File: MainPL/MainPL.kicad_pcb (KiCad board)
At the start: 2 copper layers, 113 x 155.6 mm, 37 parts, among them J1 Conn_01x06_Female, J10 Conn_01x06_Female, J11 Conn_01x06_Female, J12 Conn_01x06_Female, J13 Conn_01x06_Female, J14 Conn_01x06_Female, J15 Conn_01x01_Male, J16 Conn_01x04_Male, J2 USB_B, J3 Conn_01x06_Female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

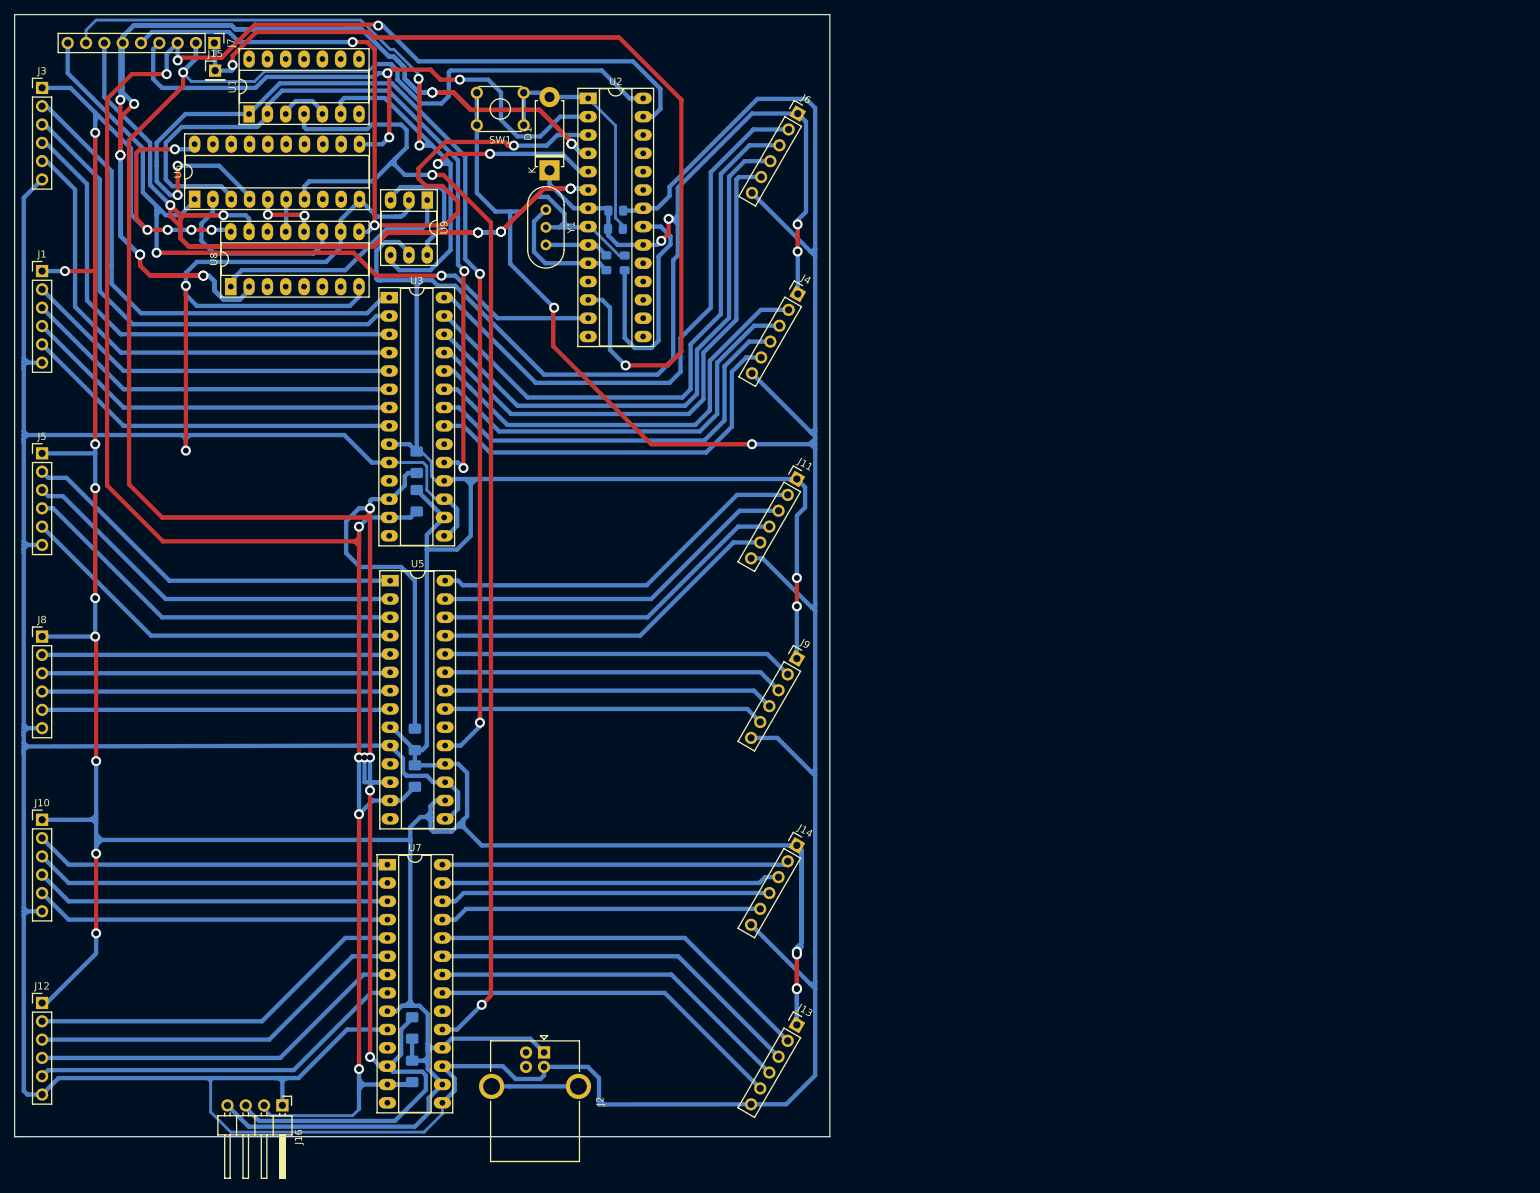
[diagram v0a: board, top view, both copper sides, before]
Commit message: Änderung der Ints und leichte Verbesserung
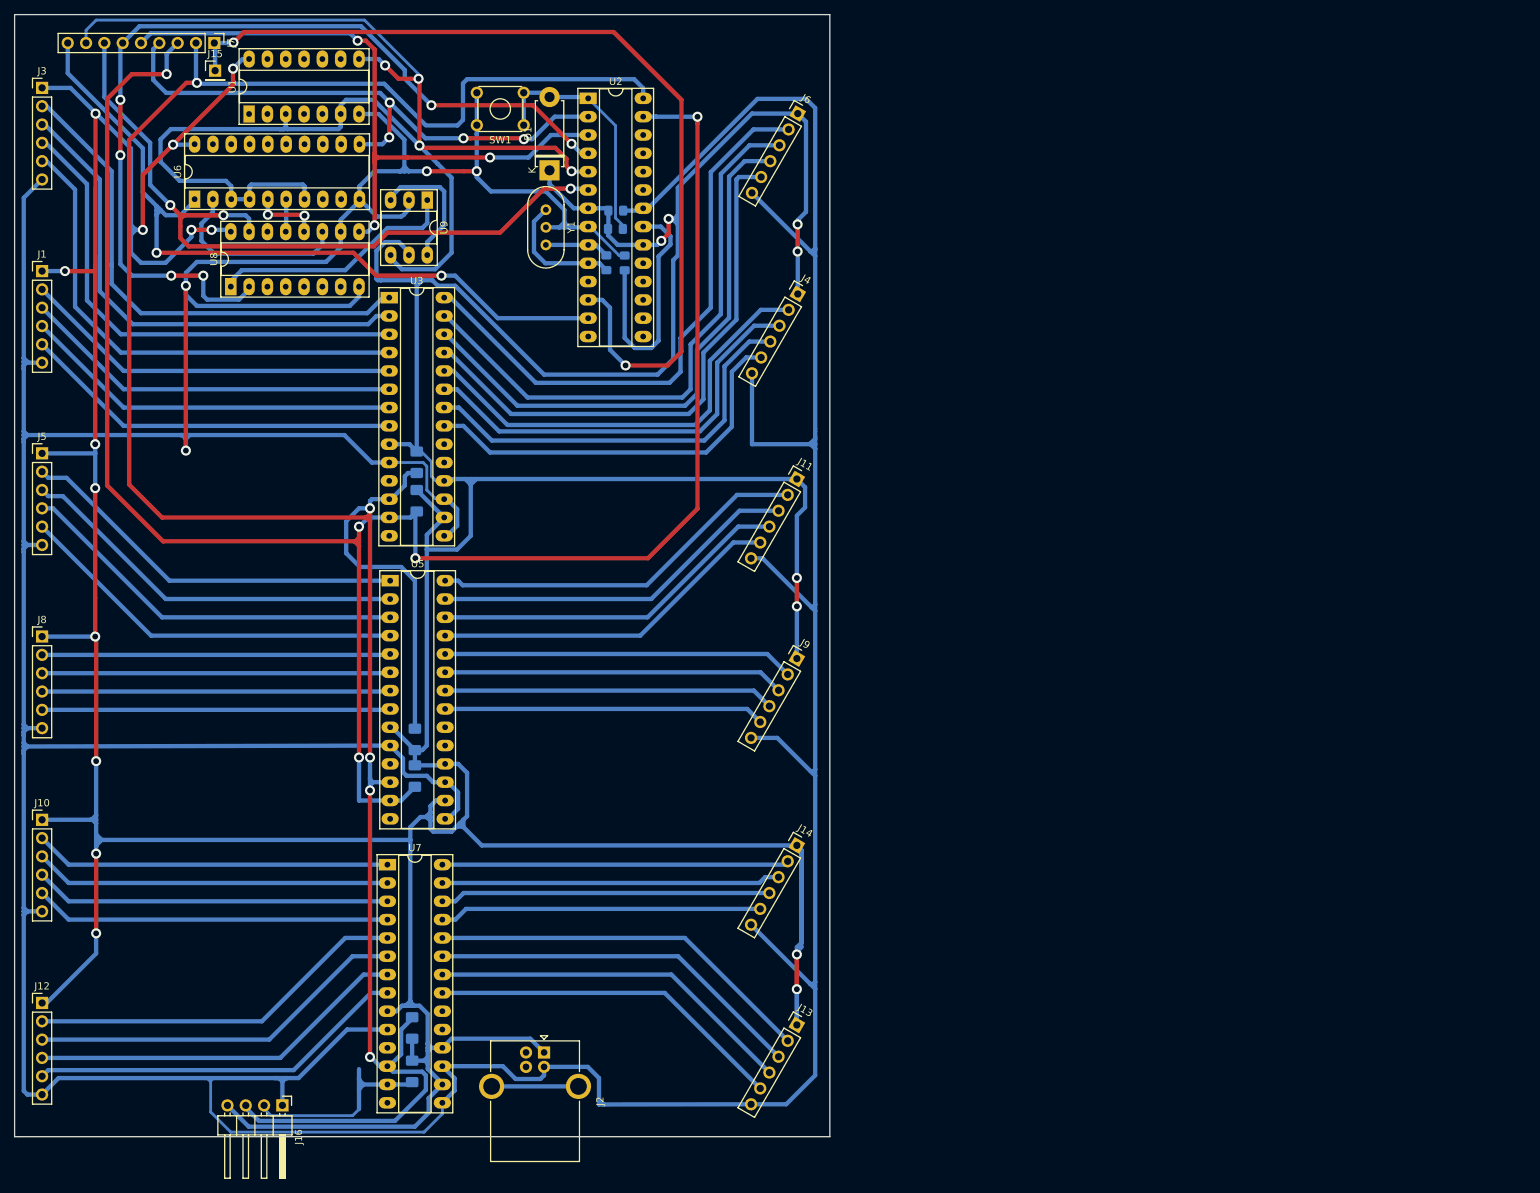
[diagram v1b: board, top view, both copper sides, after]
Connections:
- U1 pad 1: /INTB_2 -> Net-(U1-Pad1)
- U1 pad 10: (no net) -> Net-(U1-Pad10)
- U1 pad 14: (no net) -> +5V
- U1 pad 2: /INTB_1 -> Net-(U1-Pad2)
- U1 pad 3: Net-(U1-Pad3) -> /INTArduino
- U1 pad 4: /INTB_3 -> Net-(U1-Pad4)
- U1 pad 5: Net-(U1-Pad3) -> /INTB_2
- U1 pad 7: (no net) -> GND
- U1 pad 8: (no net) -> /INTArduino
- U1 pad 9: (no net) -> Net-(U1-Pad9)
- U3 pad 19: /INTB_1 -> Net-(U1-Pad2)
- U3 pad 20: Net-(U3-Pad20) -> Net-(U1-Pad1)
- U5 pad 20: Net-(U5-Pad20) -> Net-(U1-Pad4)
- U6 pad 3: /INTB_1 -> /INTArduino
- U6 pad 4: /INTB_2 -> /INTArduino
- U6 pad 7: /INTB_3 -> /INTArduino
- U7 pad 19: /INTB_3 -> Net-(U1-Pad10)
- U7 pad 20: Net-(U7-Pad20) -> Net-(U1-Pad9)
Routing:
- net /INTB_3: track 171.8 -> 0.00 mm, vias 2 -> 0
- net /INTB_2: track 161.4 -> 0.00 mm, vias 4 -> 0
- net /CLK: track 252.7 -> 127.1 mm, vias 12 -> 6
- net /INTB_1: track 110.1 -> 0.00 mm, vias 2 -> 0
- net /INTArduino: track 133.5 -> 200.2 mm
- net /CLK_INH: track 175.6 -> 110.0 mm, vias 8 -> 3
- net GND: track 899.7 -> 870.7 mm
- net +5V: track 834.9 -> 858.4 mm, vias 24 -> 21
- net /Qh: track 108.8 -> 93.4 mm
- net /SDA: track 317.9 -> 305.2 mm, vias 7 -> 5
- net /SCL: track 364.4 -> 352.1 mm, vias 6 -> 5
- net /LE: track 88.3 -> 79.8 mm, vias 3 -> 4
- net Net-(U1-Pad3): track 7.04 -> 0.00 mm
- net Servo: track 131.6 -> 129.0 mm

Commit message: MainPL fertig
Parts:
- moved U9 1.21 mm to (102.9, 51.8)
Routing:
- net Net-(U1-Pad10): track 0.00 -> 227.8 mm, vias 0 -> 2
- net /INTB_2: track 0.00 -> 227.4 mm, vias 0 -> 4
- net Net-(U1-Pad4): track 0.00 -> 220.3 mm, vias 0 -> 4
- net Net-(U1-Pad9): track 0.00 -> 217.7 mm, vias 0 -> 2
- net Net-(U1-Pad2): track 0.00 -> 144.1 mm, vias 0 -> 4
- net Net-(U1-Pad1): track 0.00 -> 102.1 mm, vias 0 -> 2
- net /SDA: track 305.2 -> 345.7 mm, vias 5 -> 6
- net +5V: track 858.4 -> 821.1 mm, vias 21 -> 20
- net /Qh: track 93.4 -> 114.1 mm, vias 3 -> 4
- net /INTArduino: track 200.2 -> 218.0 mm, vias 4 -> 7
- net /LE: track 79.8 -> 90.5 mm, vias 4 -> 3
- net Net-(U9-Pad3): track 18.5 -> 9.72 mm
- net Net-(U8-Pad1): track 34.5 -> 41.1 mm, vias 0 -> 2
- net Servo: track 129.0 -> 133.2 mm
- net GND: track 870.7 -> 867.7 mm
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- added copper zone on B.Cu, net GND
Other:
- board text added: "M.S Main Platine V1.0"

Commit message: Add files via upload
V.2 von Parkplatz mit neuen Maßen
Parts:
- removed J14, J4, J9: Conn_01x06_Female, Connector_PinHeader_2.54mm:PinHeader_1x06_P2.54mm_Vertical
- added Je: Conn_01x06_Female, Connector_PinHeader_2.54mm:PinHeader_1x06_P2.54mm_Vertical, F.Cu at (122.6, 35.6)
- added Je: Conn_01x06_Female, Connector_PinHeader_2.54mm:PinHeader_1x06_P2.54mm_Vertical, F.Cu at (182.1, 35.6)
- added Je: Conn_01x06_Female, Connector_PinHeader_2.54mm:PinHeader_1x06_P2.54mm_Vertical, F.Cu at (211.8, 35.6)
- added SW2: SW_Push_MS, Button_Switch_THT:SW_TH_Tactile_Omron_B3F-10xx, F.Cu at (56.6, 71.1)
- SW1: value SW_Push_Dual -> SW_Push_MS
- moved J16 174.8 mm to (240.3, 103.9), turned to 0 degrees
- moved J2 157.6 mm to (238.8, 68.8), turned to 0 degrees
- moved R6 150.9 mm to (225.1, 88.9), turned to 0 degrees
- moved J12 149.9 mm to (196.3, 139.7), turned to 90 degrees
- moved R8 142.5 mm to (219.1, 88.9), turned to 0 degrees
- moved J10 120.9 mm to (169.2, 139.7), turned to 90 degrees
- moved U7 112.8 mm to (196.5, 92.3), turned to 90 degrees
- moved J3 104.3 mm to (61.0, 139.7), turned to 90 degrees
- moved J8 97.9 mm to (142.2, 139.7), turned to 90 degrees
- moved J7 88.5 mm to (51.8, 116.1), turned to 0 degrees
- moved J1 87.8 mm to (88.4, 139.7), turned to 90 degrees
- moved J5 85.4 mm to (115.3, 139.7), turned to 90 degrees
- moved R3 84.5 mm to (172.8, 88.8), turned to 0 degrees
- moved J15 83.8 mm to (55.6, 116.0), turned to 90 degrees
- moved R4 77.5 mm to (167.7, 88.8), turned to 0 degrees
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- renumbered J11 to Je
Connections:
- net /INTB_2 renamed Net-(U1-Pad5)
- SW1 pad 1: Net-(D1-Pad2) -> Net-(SW1-Pad1)
- SW1 pad 2: GND -> Net-(SW1-Pad1)
- SW1 pad 3: Net-(D1-Pad2) -> GND
- U2 pad 14: Net-(U2-Pad14) -> Net-(SW1-Pad1)
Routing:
- net Net-(U1-Pad10): track 227.8 -> 0.00 mm, vias 2 -> 0
- net Net-(U1-Pad5): track 227.4 -> 0.00 mm, vias 4 -> 0
- net Net-(U1-Pad4): track 220.3 -> 0.00 mm, vias 4 -> 0
- net Net-(U1-Pad9): track 217.7 -> 0.00 mm, vias 2 -> 0
- net /SDA: track 345.7 -> 145.1 mm, vias 6 -> 3
- net /INTArduino: track 218.0 -> 19.3 mm, vias 7 -> 0
- net /SCL: track 350.5 -> 158.8 mm, vias 4 -> 3
- net +5V: track 821.1 -> 661.1 mm, vias 20 -> 0
- net Net-(U1-Pad2): track 144.1 -> 0.00 mm, vias 4 -> 0
- net Servo: track 133.2 -> 3.88 mm, vias 2 -> 0
- net /CLK: track 126.1 -> 0.00 mm, vias 6 -> 0
- net /Qh: track 114.1 -> 0.00 mm, vias 4 -> 0
- net /CLK_INH: track 108.7 -> 0.00 mm, vias 3 -> 0
- net /OE: track 106.8 -> 0.00 mm, vias 2 -> 0
- net Net-(U1-Pad1): track 102.1 -> 0.00 mm, vias 2 -> 0
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- removed copper zone on B.Cu, net GND
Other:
- board size 113 x 155.6 mm -> 200 x 113 mm
- rule trace_min: 0.6 -> 0.4
- board text removed: "M.S Main Platine V1.0"

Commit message: Neues Pcb fertig
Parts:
- moved U1 135.1 mm to (189.7, 63.8), turned to 0 degrees
- moved U9 43.1 mm to (89.7, 117.9), turned to 270 degrees
- moved U6 4.75 mm to (72.6, 114.0)
- moved U8 3.78 mm to (89.7, 113.0)
- moved J7 1.80 mm to (53.6, 115.8)
- moved J15 1.76 mm to (57.4, 115.8)
- moved SW2 0.96 mm to (57.2, 71.9)
- moved SW1 0.40 mm to (89.6, 59.2)
- renumbered Je to J11, Je to J14, Je to J4, Je to J9
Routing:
- net /INTArduino: track 19.3 -> 308.9 mm, vias 0 -> 4
- net +5V: track 661.1 -> 922.5 mm, vias 0 -> 3
- net /SDA: track 145.1 -> 336.6 mm, vias 3 -> 5
- net /SCL: track 158.8 -> 336.6 mm, vias 3 -> 5
- net Servo: track 3.88 -> 141.1 mm, vias 0 -> 2
- net /CLK: track 0.00 -> 133.3 mm, vias 0 -> 4
- net /Qh: track 0.00 -> 130.6 mm, vias 0 -> 2
- net /OE: track 0.00 -> 129.3 mm, vias 0 -> 4
- net /CLK_INH: track 0.00 -> 104.1 mm, vias 0 -> 5
- net Net-(U1-Pad1): track 0.00 -> 90.9 mm, vias 0 -> 2
- net Net-(U1-Pad2): track 0.00 -> 86.1 mm, vias 0 -> 2
- net /LE: track 0.00 -> 81.5 mm
- net GND: track 874.2 -> 945.5 mm
- net Net-(U6-Pad2): track 0.00 -> 33.5 mm
- net Net-(U6-Pad5): track 0.00 -> 33.2 mm
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- added copper zone on F.Cu, net (none)
- added copper zone on B.Cu, net GND

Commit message: neues Pcb fertig
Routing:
- net GND: track 945.5 -> 924.0 mm
- net /DATA11: track 74.5 -> 87.5 mm, vias 1 -> 2
- net /B11: track 76.7 -> 83.7 mm, vias 1 -> 2
- net /INTArduino: track 308.9 -> 313.7 mm
- net /CLK_INH: track 104.1 -> 108.3 mm
- net /SCL: track 336.6 -> 338.6 mm
- net /SDA: track 336.6 -> 337.8 mm
- net /G11: track 79.1 -> 80.1 mm, vias 1 -> 2
- net /OE: track 129.3 -> 130.0 mm
- net /R11: track 81.3 -> 81.4 mm, vias 1 -> 2

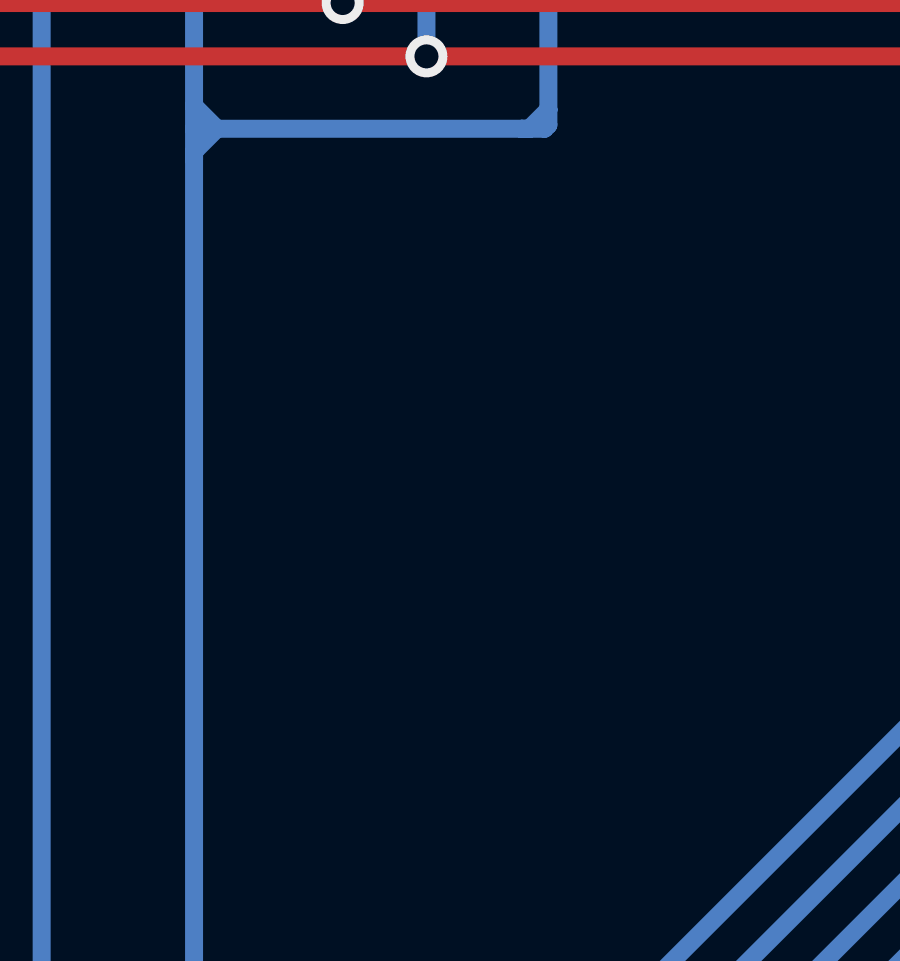
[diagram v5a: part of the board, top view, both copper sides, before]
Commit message: Beschriftung eingefügt
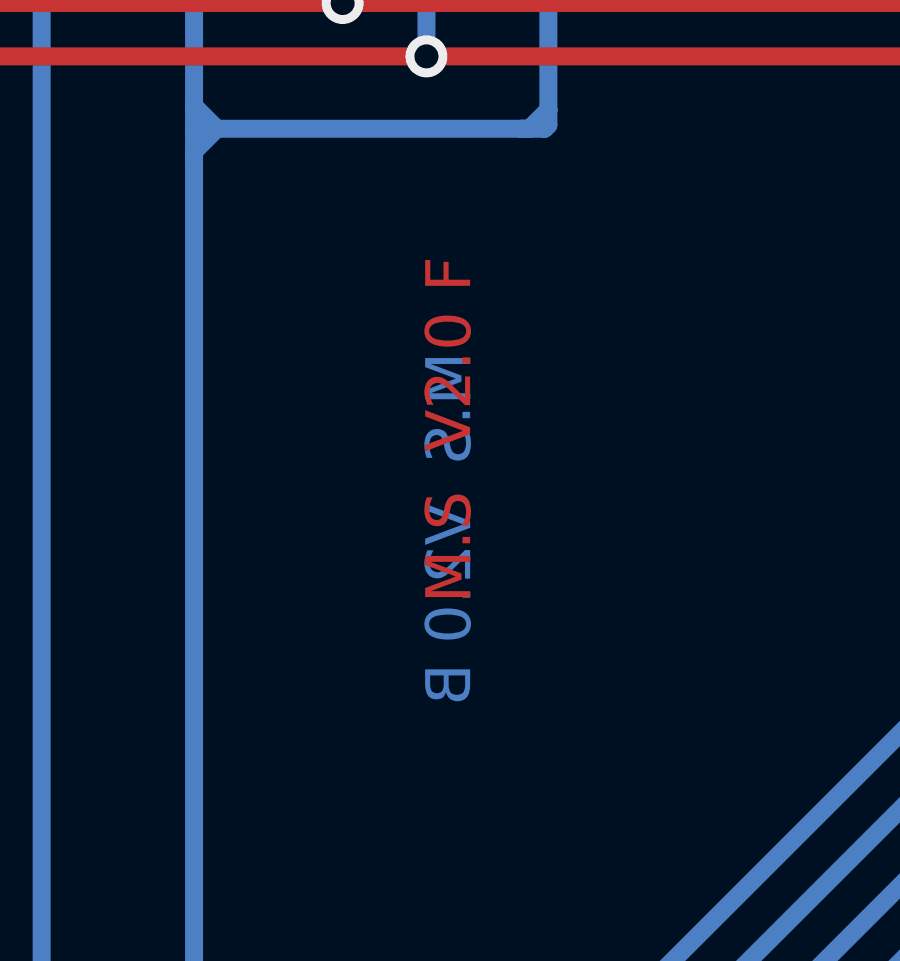
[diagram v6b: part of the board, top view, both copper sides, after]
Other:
- board text added: "M.S V2.0 B"
- board text added: "M.S V2.0 F"
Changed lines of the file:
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@@
   (general
     (thickness 1.6)
-    (drawings 23)
+    (drawings 25)
     (tracks 980)
     (zones 0)
@@
     )
   )
+  (gr_text "M.S  V2.0 F" (at 177.292 108.966 90) (layer F.Cu)
+    (effects (font (size 1.5 1.5) (thickness 0.3)))
+  )
+  (gr_text "M.S  V2.0 B" (at 177.292 112.268 90) (layer B.Cu)
+    (effects (font (size 1.5 1.5) (thickness 0.3)) (justify mirror))
+  )
   (dimension 11.303 (width 0.15) (layer Dwgs.User)
